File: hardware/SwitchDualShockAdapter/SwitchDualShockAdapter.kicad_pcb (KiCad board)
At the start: 2 copper layers, 54.6 x 48.3 mm, 30 parts, among them J1 USB, J2 USB_C_Receptacle, J3 DualShockSocket, J4 Serial, U1 ATmega8A-P, U2 LP2950-3.3_TO92

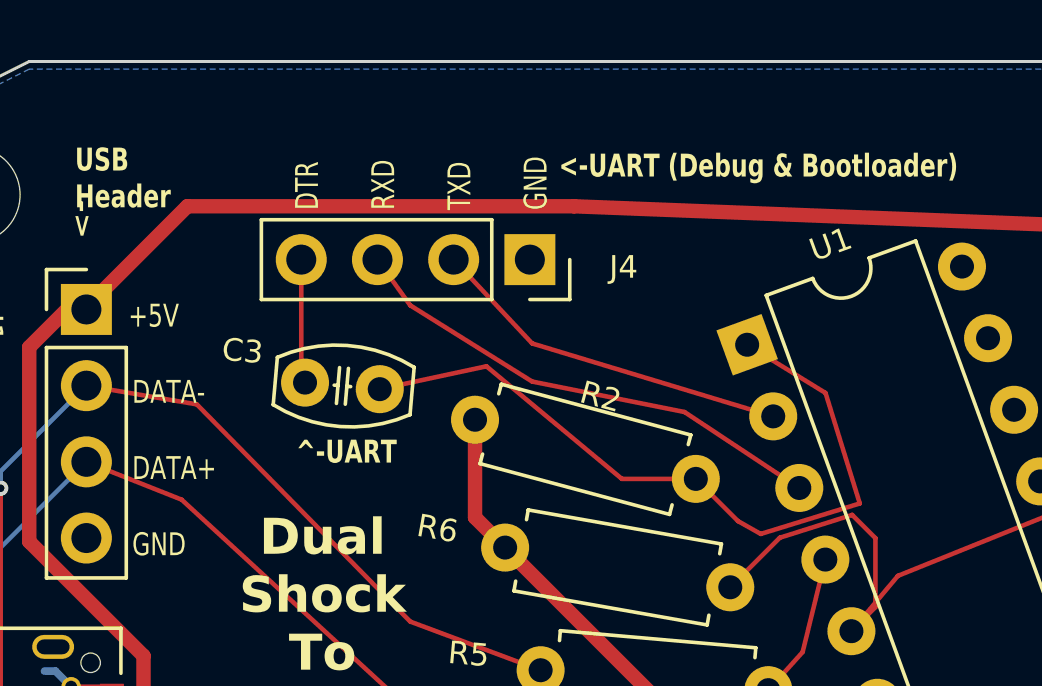
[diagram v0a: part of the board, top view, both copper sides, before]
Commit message: Flip serial header to more intuitive orientation. Fix the debug LED to be in the correct orientation.
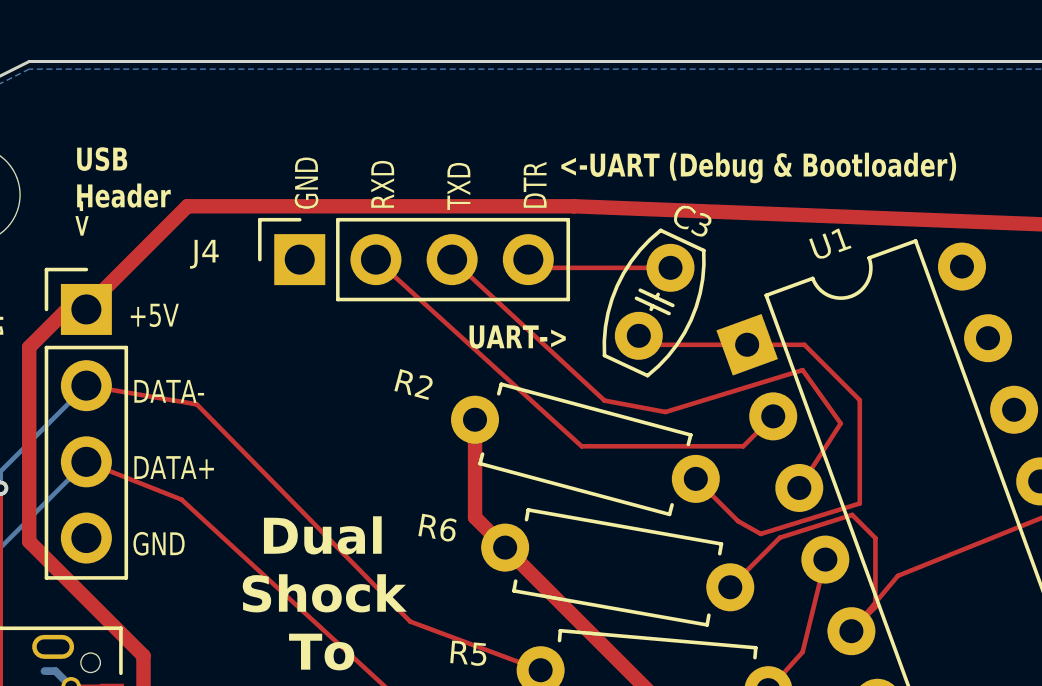
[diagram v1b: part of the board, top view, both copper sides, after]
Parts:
- moved C3 8.82 mm to (167.6, 75.2), turned to 65 degrees
- moved J4 7.67 mm to (156.3, 72.6), turned to 90 degrees
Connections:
- J2 pad 31: (no net) -> Net-(J2-SHIELD)
- J2 pad 32: (no net) -> Net-(J2-SHIELD)
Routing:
- net /~RESET: track 25.2 -> 18.0 mm
- net /RXD: track 12.2 -> 16.1 mm
- net /TXD: track 16.4 -> 18.5 mm
- net /DTR: track 3.97 -> 4.85 mm
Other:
- board text added: "UART->"
- board text removed: "^-UART"

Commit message: Bump version number on PCB.
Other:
- board text added: "V1.1"
- board text removed: "V1.0"
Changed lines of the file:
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@@
     )
   )
-  (gr_text "V1.0" (at 160.02 89.154) (layer "F.SilkS")
+  (gr_text "V1.1" (at 160.02 89.154) (layer "F.SilkS")
     (effects (font (face "Sinclair ZX Spectrum ES") (size 0.754 0.754) (thickness 0.09425)))
-    (render_cache "V1.0" 0
+    (render_cache "V1.1" 0
       (polygon
         (pts
-          (xy 158.602159 89.335052)          (xy 158.602159 89.20301)          (xy 158.866059 89.20301)          (xy 158.866059 89.335052)
+          (xy 158.56901 89.335052)          (xy 158.56901 89.20301)          (xy 158.83291 89.20301)          (xy 158.83291 89.335052)
         )
       )
       (polygon
         (pts
-          (xy 158.470302 89.20301)          (xy 158.470302 89.071152)          (xy 158.602159 89.071152)          (xy 158.602159 89.20301)
+          (xy 158.437153 89.20301)          (xy 158.437153 89.071152)          (xy 158.56901 89.071152)          (xy 158.56901 89.20301)
         )
       )
       (polygon
         (pts
-          (xy 158.866059 89.20301)          (xy 158.866059 89.071152)          (xy 158.998102 89.071152)          (xy 158.998102 89.20301)
+          (xy 158.83291 89.20301)          (xy 158.83291 89.071152)          (xy 158.964953 89.071152)          (xy 158.964953 89.20301)
         )
       )
       (polygon
         (pts
-          (xy 158.338259 89.071152)          (xy 158.338259 88.543352)          (xy 158.470302 88.543352)          (xy 158.470302 89.071152)
+          (xy 158.30511 89.071152)          (xy 158.30511 88.543352)          (xy 158.437153 88.543352)          (xy 158.437153 89.071152)
         )
       )
       (polygon
         (pts
-          (xy 158.998102 89.071152)          (xy 158.998102 88.543352)          (xy 159.129959 88.543352)          (xy 159.129959 89.071152)
+          (xy 158.964953 89.071152)          (xy 158.964953 88.543352)          (xy 159.09681 88.543352)          (xy 159.09681 89.071152)
         )
       )
       (polygon
         (pts
-          (xy 159.459604 88.807252)          (xy 159.459604 88.67521)          (xy 159.591462 88.67521)          (xy 159.591462 88.807252)
+          (xy 159.426455 88.807252)          (xy 159.426455 88.67521)          (xy 159.558313 88.67521)          (xy 159.558313 88.807252)
         )
       )
       (polygon
         (pts
-          (xy 159.459604 89.335052)          (xy 159.459604 89.20301)          (xy 159.723504 89.20301)          (xy 159.723504 88.67521)
-          (xy 159.591462 88.67521)          (xy 159.591462 88.543352)          (xy 159.855362 88.543352)          (xy 159.855362 89.20301)
-          (xy 160.119262 89.20301)          (xy 160.119262 89.335052)
+          (xy 159.426455 89.335052)          (xy 159.426455 89.20301)          (xy 159.690355 89.20301)          (xy 159.690355 88.67521)
+          (xy 159.558313 88.67521)          (xy 159.558313 88.543352)          (xy 159.822213 88.543352)          (xy 159.822213 89.20301)
+          (xy 160.086113 89.20301)          (xy 160.086113 89.335052)
         )
       )
       (polygon
         (pts
-          (xy 160.580765 89.335052)          (xy 160.580765 89.071152)          (xy 160.844665 89.071152)          (xy 160.844665 89.335052)
+          (xy 160.547616 89.335052)          (xy 160.547616 89.071152)          (xy 160.811516 89.071152)          (xy 160.811516 89.335052)
         )
       )
       (polygon
         (pts
-          (xy 161.372281 88.93911)          (xy 161.372281 88.807252)          (xy 161.504323 88.807252)          (xy 161.504323 88.93911)
+          (xy 161.141345 88.807252)          (xy 161.141345 88.67521)          (xy 161.273203 88.67521)          (xy 161.273203 88.807252)
         )
       )
       (polygon
         (pts
-          (xy 161.174494 89.335052)          (xy 161.174494 89.20301)          (xy 161.042452 89.20301)          (xy 161.042452 88.67521)
-          (xy 161.174494 88.67521)          (xy 161.174494 89.071152)          (xy 161.240423 89.071152)          (xy 161.240423 88.93911)
-          (xy 161.372281 88.93911)          (xy 161.372281 89.071152)          (xy 161.306352 89.071152)          (xy 161.306352 89.20301)
-          (xy 161.636365 89.20301)          (xy 161.636365 88.807252)          (xy 161.504323 88.807252)          (xy 161.504323 88.67521)
-          (xy 161.174494 88.67521)          (xy 161.174494 88.543352)          (xy 161.636365 88.543352)          (xy 161.636365 88.67521)
-          (xy 161.768223 88.67521)          (xy 161.768223 89.20301)          (xy 161.702294 89.20301)          (xy 161.702294 89.335052)
+          (xy 161.141345 89.335052)          (xy 161.141345 89.20301)          (xy 161.405245 89.20301)          (xy 161.405245 88.67521)
+          (xy 161.273203 88.67521)          (xy 161.273203 88.543352)          (xy 161.537103 88.543352)          (xy 161.537103 89.20301)
+          (xy 161.801003 89.20301)          (xy 161.801003 89.335052)
         )
       )
